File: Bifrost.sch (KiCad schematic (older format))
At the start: 44 parts, among them IC1 DS1085Z-10+, IC2 DS1085Z-10+, J1 OIP, J10 Barrel_Jack_Switch, J5 CalCK, U5 74AHC1G04, U6 74AHC1G04

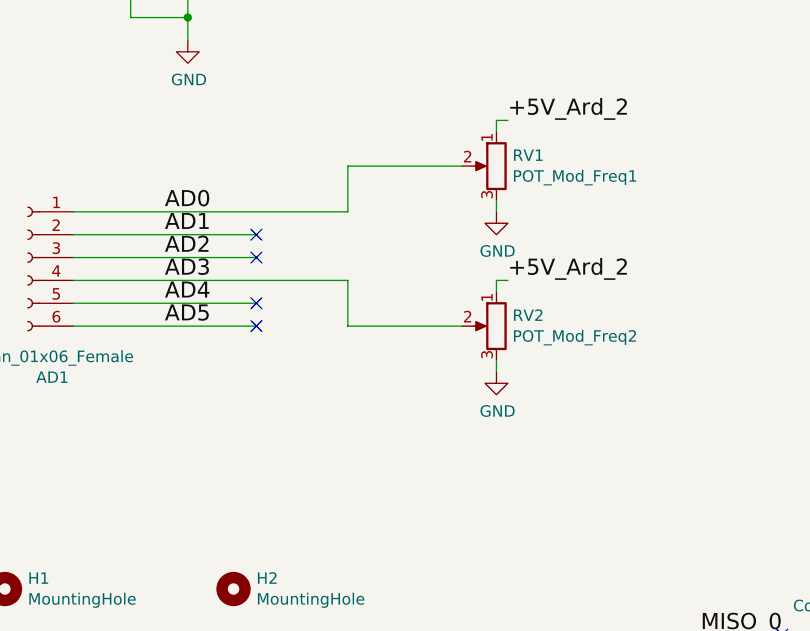
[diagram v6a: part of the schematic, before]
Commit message: Added capacitors on potars
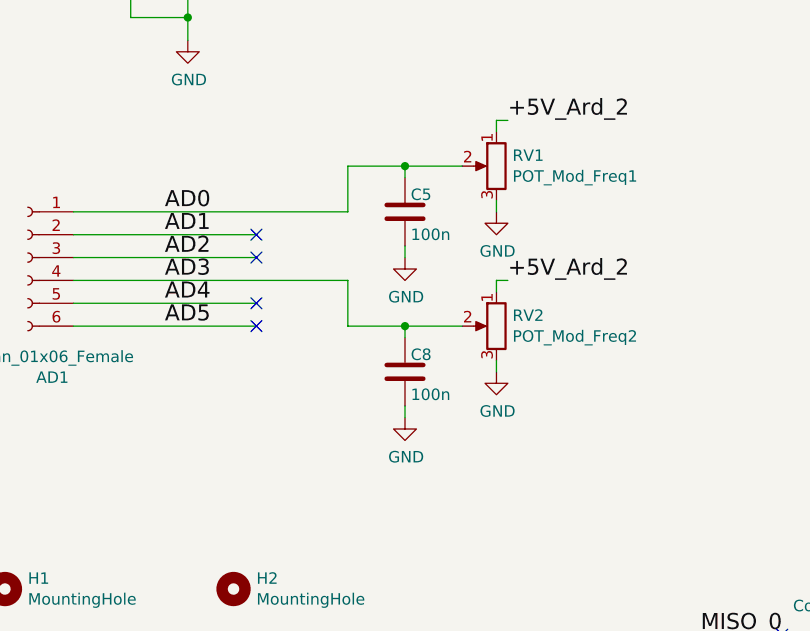
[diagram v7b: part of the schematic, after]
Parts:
- added C5, C8: 100n, Capacitor_SMD:C_0603_1608Metric_Pad1.08x0.95mm_HandSolder, symbol Device:C
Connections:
- net AD0: now also C5.2
- net AD3: now also C8.2
- net GND: now also C5.1, C8.1
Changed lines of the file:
@@
 	2850 5850 2850 5800
-Wire Wire Line
-	2200 6000 2700 6000
 Wire Wire Line
 	1800 6000 1000 6000
@@
 Wire Wire Line
 	1000 5500 2200 5500
-Wire Wire Line
-	2700 5300 2200 5300
 Wire Wire Line
 	2850 5150 2850 5100
@@
 	0    -1   -1   0
 $EndComp
+$Comp
+L Device:C C?
+U 1 1 610B501D
+P 2450 5500
+AR Path="/60D21B6E/610B501D" Ref="C?"  Part="1"
+AR Path="/610B501D" Ref="C5"  Part="1"
+F 0 "C5" H 2425 5425 50  0000 R CNN
+F 1 "100n" H 2425 5600 50  0000 R CNN
+F 2 "Capacitor_SMD:C_0603_1608Metric_Pad1.08x0.95mm_HandSolder" H 2488 5350 50  0001 C CNN
+F 3 "~" H 2450 5500 50  0001 C CNN
+	1    2450 5500
+	-1   0    0    1
+$EndComp
+$Comp
+L Device:C C?
+U 1 1 610C4CF3
+P 2450 6200
+AR Path="/60D21B6E/610C4CF3" Ref="C?"  Part="1"
+AR Path="/610C4CF3" Ref="C8"  Part="1"
+F 0 "C8" H 2425 6125 50  0000 R CNN
+F 1 "100n" H 2425 6300 50  0000 R CNN
+F 2 "Capacitor_SMD:C_0603_1608Metric_Pad1.08x0.95mm_HandSolder" H 2488 6050 50  0001 C CNN
+F 3 "~" H 2450 6200 50  0001 C CNN
+	1    2450 6200
+	-1   0    0    1
+$EndComp
+Wire Wire Line
+	2200 6000 2450 6000
+Wire Wire Line
+	2200 5300 2450 5300
+Wire Wire Line
+	2450 5350 2450 5300
+Connection ~ 2450 5300
+Wire Wire Line
+	2450 5300 2700 5300
+Wire Wire Line
+	2450 6050 2450 6000
+Connection ~ 2450 6000
+Wire Wire Line
+	2450 6000 2700 6000
+$Comp
+L power:GND #PWR?
+U 1 1 610FEE20
+P 2450 5700
+AR Path="/60D21B6E/610FEE20" Ref="#PWR?"  Part="1"
+AR Path="/610FEE20" Ref="#PWR0110"  Part="1"
+F 0 "#PWR0110" H 2450 5450 50  0001 C CNN
+F 1 "GND" H 2455 5527 50  0000 C CNN
+F 2 "" H 2450 5700 50  0001 C CNN
+F 3 "" H 2450 5700 50  0001 C CNN
+	1    2450 5700
+	1    0    0    -1
+$EndComp
+Wire Wire Line
+	2450 5650 2450 5700
+$Comp
+L power:GND #PWR?
+U 1 1 6110A595
+P 2450 6400
+AR Path="/60D21B6E/6110A595" Ref="#PWR?"  Part="1"
+AR Path="/6110A595" Ref="#PWR0111"  Part="1"
+F 0 "#PWR0111" H 2450 6150 50  0001 C CNN
+F 1 "GND" H 2455 6227 50  0000 C CNN
+F 2 "" H 2450 6400 50  0001 C CNN
+F 3 "" H 2450 6400 50  0001 C CNN
+	1    2450 6400
+	1    0    0    -1
+$EndComp
+Wire Wire Line
+	2450 6350 2450 6400
 $EndSCHEMATC

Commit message: As implemented for v1
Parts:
- removed R1, R2: 510, Resistor_SMD:R_0603_1608Metric_Pad0.98x0.95mm_HandSolder, symbol Device:R
- removed R19, R5: 0, Resistor_SMD:R_0603_1608Metric_Pad0.98x0.95mm_HandSolder, symbol Device:R
- added C? (x4): 1u, Capacitor_SMD:C_0603_1608Metric_Pad1.08x0.95mm_HandSolder, symbol Device:C
- R10, R9: value 0 -> 0 NP
- R13: value 510 -> DEPOP (510)
- R6: value 510 -> (510) DEPOP
- U5, U6: value 74AHC1G04 -> NP 74AHC1G04
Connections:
- net Sheet60D21B6D/InI+: now also C?.2
- net Sheet60D21B6D/InQ+: now also C?.2
- net Sheet60D21B6D/OutI+: now also C?.1
- net Sheet60D21B6D/OutQ+: now also C?.1
- net at J1.1 (In), R13.1, R6.2: now also C?.2, C?.2
- net at R4.2, U5.4: now also C?.1
- net at R17.2, U6.4: now also C?.1
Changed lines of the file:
@@
 Wire Wire Line
 	1250 4500 1250 4650
-$Comp
-L Device:R R1
-U 1 1 611AF28E
-P 8750 2150
-F 0 "R1" V 8700 2350 50  0000 C CNN
-F 1 "510" V 8750 2150 50  0000 C CNN
-F 2 "Resistor_SMD:R_0603_1608Metric_Pad0.98x0.95mm_HandSolder" V 8680 2150 50  0001 C CNN
-F 3 "~" H 8750 2150 50  0001 C CNN
-	1    8750 2150
-	0    1    1    0
-$EndComp
-$Comp
-L Device:R R2
-U 1 1 611BB3A9
-P 8750 2450
-F 0 "R2" V 8700 2650 50  0000 C CNN
-F 1 "510" V 8750 2450 50  0000 C CNN
-F 2 "Resistor_SMD:R_0603_1608Metric_Pad0.98x0.95mm_HandSolder" V 8680 2450 50  0001 C CNN
-F 3 "~" H 8750 2450 50  0001 C CNN
-	1    8750 2450
-	0    1    1    0
-$EndComp
 Wire Wire Line
 	9650 2150 9650 2300
@@
 	-1   0    0    1
 $EndComp
-$Comp
-L Device:R R5
-U 1 1 612C3DB1
-P 6350 1750
-F 0 "R5" V 6450 1750 50  0000 C CNN
-F 1 "0" V 6350 1750 50  0000 C CNN
-F 2 "Resistor_SMD:R_0603_1608Metric_Pad0.98x0.95mm_HandSolder" V 6280 1750 50  0001 C CNN
-F 3 "~" H 6350 1750 50  0001 C CNN
-	1    6350 1750
-	0    1    1    0
-$EndComp
 Wire Wire Line
 	6200 1750 6150 1750
@@
 P 8950 2650
 F 0 "R13" V 9050 2650 50  0000 C CNN
-F 1 "510" V 8950 2650 50  0000 C CNN
+F 1 "DEPOP (510)" V 8950 2500 50  0000 C CNN
 F 2 "Resistor_SMD:R_0603_1608Metric_Pad0.98x0.95mm_HandSolder" V 8880 2650 50  0001 C CNN
 F 3 "~" H 8950 2650 50  0001 C CNN
@@
 Wire Wire Line
 	6150 1250 6150 1400
-$Comp
-L Device:R R19
-U 1 1 6137D7BA
-P 6350 2900
-F 0 "R19" V 6450 2900 50  0000 C CNN
-F 1 "0" V 6350 2900 50  0000 C CNN
-F 2 "Resistor_SMD:R_0603_1608Metric_Pad0.98x0.95mm_HandSolder" V 6280 2900 50  0001 C CNN
-F 3 "~" H 6350 2900 50  0001 C CNN
-	1    6350 2900
-	0    1    1    0
-$EndComp
 Wire Wire Line
 	5250 2950 5250 2900
@@
 P 5600 1750
 F 0 "U5" H 5350 2050 50  0000 C CNN
-F 1 "74AHC1G04" H 5350 1950 50  0000 C CNN
+F 1 "NP 74AHC1G04" H 5775 1575 50  0000 C CNN
 F 2 "Package_TO_SOT_SMD:SOT-353_SC-70-5" H 5600 1750 50  0001 C CNN
 F 3 "http://www.ti.com/lit/sg/scyt129e/scyt129e.pdf" H 5600 1750 50  0001 C CNN
@@
 P 5600 2900
 F 0 "U6" H 5350 3200 50  0000 C CNN
-F 1 "74AHC1G04" H 5350 3100 50  0000 C CNN
+F 1 "NP 74AHC1G04" H 5750 3050 50  0000 C CNN
 F 2 "Package_TO_SOT_SMD:SOT-353_SC-70-5" H 5600 2900 50  0001 C CNN
 F 3 "http://www.ti.com/lit/sg/scyt129e/scyt129e.pdf" H 5600 2900 50  0001 C CNN
@@
 P 8950 1950
 F 0 "R6" V 9050 1950 50  0000 C CNN
-F 1 "510" V 8950 1950 50  0000 C CNN
+F 1 "(510) DEPOP" V 8950 2100 50  0000 C CNN
 F 2 "Resistor_SMD:R_0603_1608Metric_Pad0.98x0.95mm_HandSolder" V 8880 1950 50  0001 C CNN
 F 3 "~" H 8950 1950 50  0001 C CNN
@@
 P 7400 1450
 F 0 "R9" V 7500 1450 50  0000 C CNN
-F 1 "0" V 7400 1450 50  0000 C CNN
+F 1 "0 NP" V 7400 1450 50  0000 C CNN
 F 2 "Resistor_SMD:R_0603_1608Metric_Pad0.98x0.95mm_HandSolder" V 7330 1450 50  0001 C CNN
 F 3 "~" H 7400 1450 50  0001 C CNN
@@
 P 7450 3750
 F 0 "R10" V 7550 3750 50  0000 C CNN
-F 1 "0" V 7450 3750 50  0000 C CNN
+F 1 "0 NP" V 7450 3750 50  0000 C CNN
 F 2 "Resistor_SMD:R_0603_1608Metric_Pad0.98x0.95mm_HandSolder" V 7380 3750 50  0001 C CNN
 F 3 "~" H 7450 3750 50  0001 C CNN
@@
 Wire Wire Line
 	2450 6350 2450 6400
+$Comp
+L Device:C C?
+U 1 1 61247E66
+P 8750 2150
+AR Path="/60D21B6E/61247E66" Ref="C?"  Part="1"
+AR Path="/61247E66" Ref="C?"  Part="1"
+F 0 "C?" H 8725 2075 50  0000 R CNN
+F 1 "1u" H 8725 2250 50  0000 R CNN
+F 2 "Capacitor_SMD:C_0603_1608Metric_Pad1.08x0.95mm_HandSolder" H 8788 2000 50  0001 C CNN
+F 3 "~" H 8750 2150 50  0001 C CNN
+	1    8750 2150
+	0    -1   -1   0
+$EndComp
+$Comp
+L Device:C C?
+U 1 1 6125DCC2
+P 8750 2450
+AR Path="/60D21B6E/6125DCC2" Ref="C?"  Part="1"
+AR Path="/6125DCC2" Ref="C?"  Part="1"
+F 0 "C?" H 8725 2375 50  0000 R CNN
+F 1 "1u" H 8725 2550 50  0000 R CNN
+F 2 "Capacitor_SMD:C_0603_1608Metric_Pad1.08x0.95mm_HandSolder" H 8788 2300 50  0001 C CNN
+F 3 "~" H 8750 2450 50  0001 C CNN
+	1    8750 2450
+	0    -1   -1   0
+$EndComp
+$Comp
+L Device:C C?
+U 1 1 61282F97
+P 6350 1750
+AR Path="/60D21B6E/61282F97" Ref="C?"  Part="1"
+AR Path="/61282F97" Ref="C?"  Part="1"
+F 0 "C?" H 6325 1675 50  0000 R CNN
+F 1 "1u" H 6325 1850 50  0000 R CNN
+F 2 "Capacitor_SMD:C_0603_1608Metric_Pad1.08x0.95mm_HandSolder" H 6388 1600 50  0001 C CNN
+F 3 "~" H 6350 1750 50  0001 C CNN
+	1    6350 1750
+	0    -1   -1   0
+$EndComp
+$Comp
+L Device:C C?
+U 1 1 61282FA1
+P 6350 2900
+AR Path="/60D21B6E/61282FA1" Ref="C?"  Part="1"
+AR Path="/61282FA1" Ref="C?"  Part="1"
+F 0 "C?" H 6325 2825 50  0000 R CNN
+F 1 "1u" H 6325 3000 50  0000 R CNN
+F 2 "Capacitor_SMD:C_0603_1608Metric_Pad1.08x0.95mm_HandSolder" H 6388 2750 50  0001 C CNN
+F 3 "~" H 6350 2900 50  0001 C CNN
+	1    6350 2900
+	0    -1   -1   0
+$EndComp
 $EndSCHEMATC
